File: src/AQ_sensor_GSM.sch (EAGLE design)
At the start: 102 parts, among them IC1 MIC29302WU, IC2 MCP73831/OT, J1 F-1X03-SIP-100-32, J3 PJ-002BH, J4 78646-3001, Q1 MMBT2222, Q2 MMBT2222, Q3 MMBT2222, Q4 MMBT2222, Q5 MMBT2222, Q6 MMBT2222, Q7 MMBT2222, U1 LM7805S/NOPB, U3 TEXAS_INSTRUMENTS_LM1117IMP-3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, U4 EC200UCNAB-N05-SNNSA, U5 TXS0108EPWR, X1 53048-08

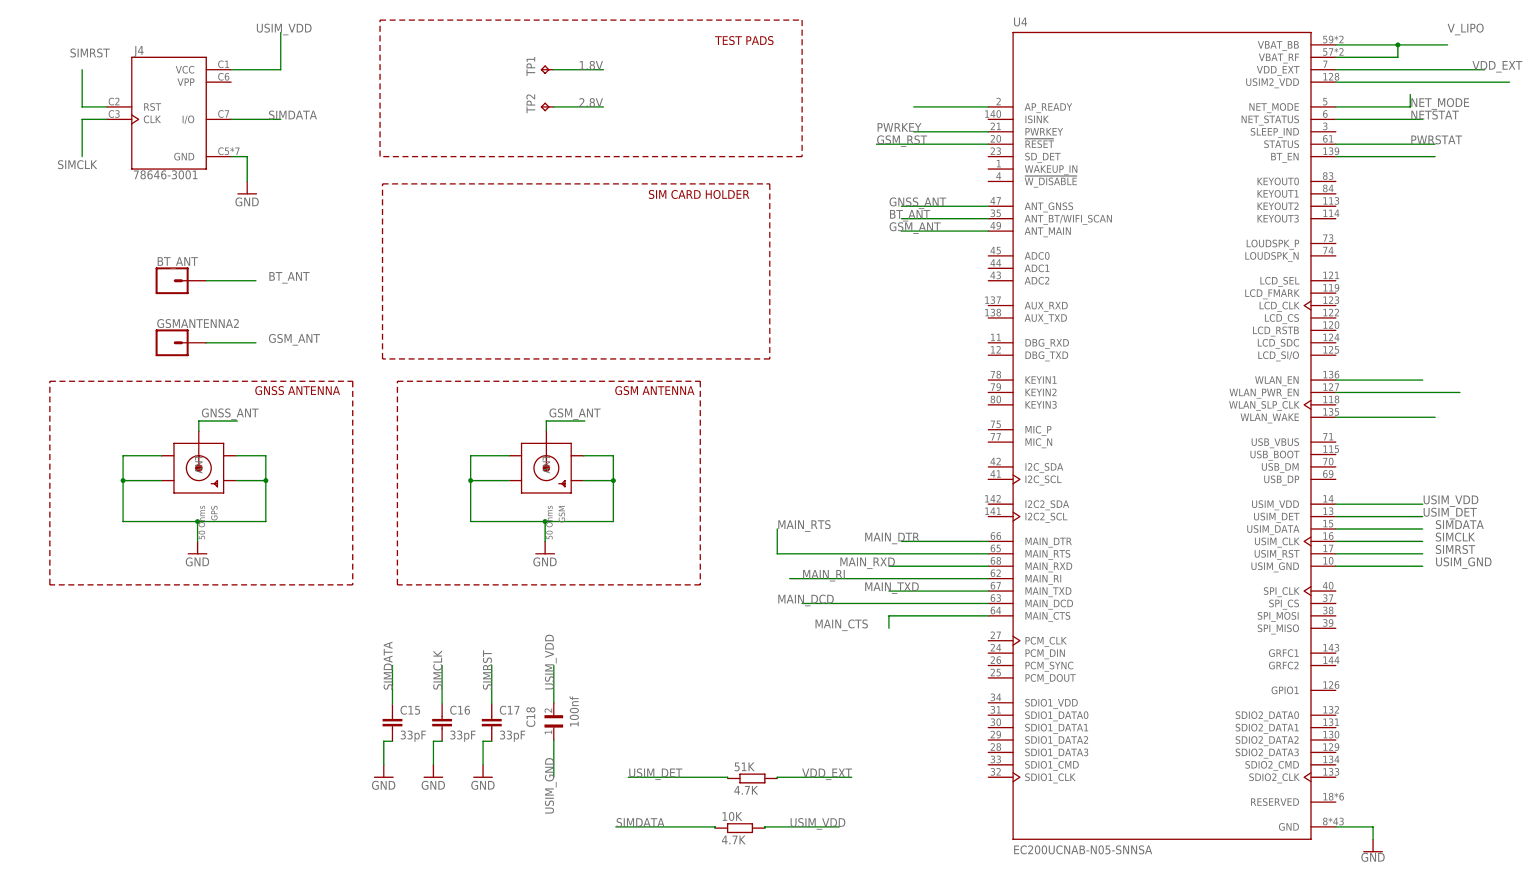
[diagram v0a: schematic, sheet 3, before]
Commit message: Replaced battery connector with 5.08mm terminal block
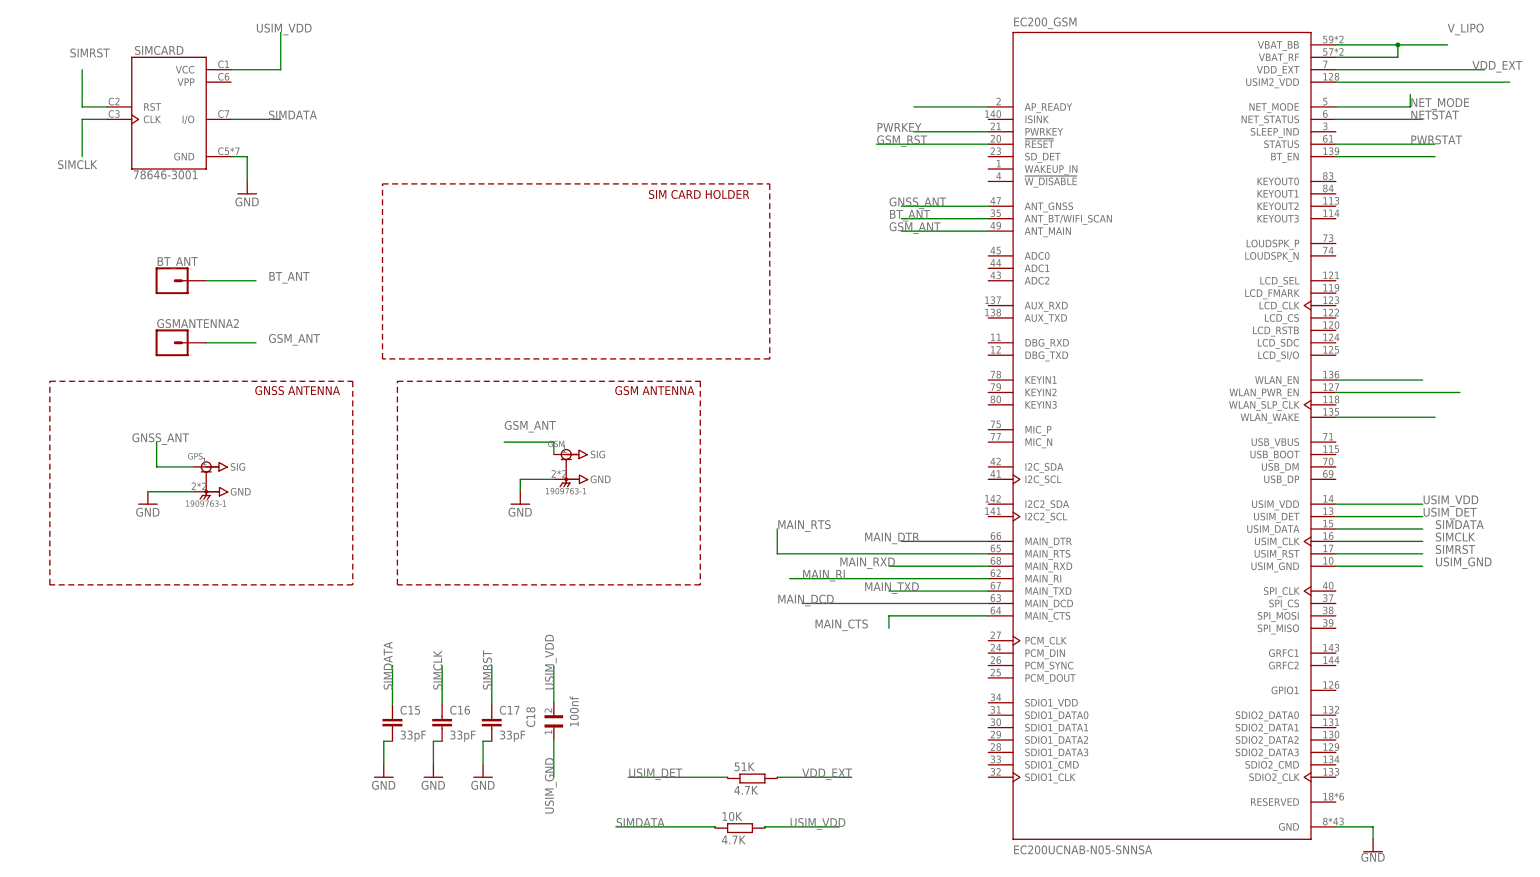
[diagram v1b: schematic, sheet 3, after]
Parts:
- removed CN1: (no value), AQ_sensor_GSM:JST_2PIN-SMT-RA
- removed TP1, TP2: TPB1,27, testpad:TPB1,27
- added 3.7V_LIPO: 2828XX-2282837-2, Connector:2828XX-2282837-2
- GPS, GSM: value 50 Ohms -> 1909763-1; device AQ_sensor_GSM:SMACONNECTOR_EDGE_UFL -> 1909763-1:1909763-1
- renumbered J4 to SIMCARD, U4 to EC200_GSM
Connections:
- removed net 1.8V: TP1.TP
- removed net 2.8V: TP2.TP
- net BP: now also 3.7V_LIPO.2; no longer CN1.2
- net GND: now also 3.7V_LIPO.1, GPS.GND, GSM.GND; no longer CN1.1, GPS.GND1, GPS.GND2, GPS.GND3, GPS.GND4, GSM.GND1, GSM.GND2, GSM.GND3, GSM.GND4
- net GNSS_ANT: now also GPS.SIG; no longer GPS.ANT
- net GSM_ANT: now also GSM.SIG; no longer GSM.ANT
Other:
- note removed: "TEST PADS"

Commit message: Added Lipo charging system
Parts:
- removed 3.7V_LIPO: 2828XX-2282837-2, Connector:2828XX-2282837-2
- removed C1, C4: 10uF, rcl:C-EUC0603
- removed CHRG: RED, led:LEDCHIP-LED0603
- removed FULL: YELLOW, led:LEDCHIP-LED0603
- removed IC2: MCP73831/OT, AQ_sensor_GSM:MCP73831/OT
- removed LIPO_SW, S1: TL2285EE, TL2285EE:TL2285EE
- removed MICRO_SD1: TF-01A, TF-01A:TF-01A
- removed MICRO_USB: 10118192-0001LF, AQ_sensor_GSM:10118192-0001LF
- removed U1: LM7805S/NOPB, LM7805S_NOPB:LM7805S/NOPB
- added 100%, 25%, 50%, 75%, C_P: ORANGE, led:LEDCHIP-LED0603
- added C14: 22nF, SparkFun-Capacitors:220PF-0402T-50V-5%
- added C21: 22pF, SparkFun-Capacitors:220PF-0402T-50V-5%
- added C22, C25, C26, C27, C5: ECA-1HM220, Resistor_Capacitor:ECA-1HM220
- added C23, C24, C29, C30: TAJB106K016RNJ, Resistor_Capacitor:TAJB106K016RNJ
- added CHARGE: PCM12SMTR, AQ_sensor_MRC:PCM12SMTR
- added L1: 784787047, Fixed Inductors:784787047
- added L2: 784778010, Fixed Inductors:784778010
- added LIPO: 2828XX-2282834-2, Connector:2828XX-2282834-2
- added LIPO/BUCK, USB/BATT: TL2285EE, TL2285EE:TL2285EE
- added PB_IN, SOLAR_IN: 10118192-0001LF, AQ_sensor_GSM:10118192-0001LF
- added R1: 110k, SparkFun-Resistors:1.20KOHM-0603-1/10W-1%
- added R37, R7: 10k, SparkFun-Resistors:1.20KOHM-0603-1/10W-1%
- added R6: 15, SparkFun-Resistors:1.20KOHM-0603-1/10W-1%
- added U$1: (no value), MT2492:MT2492MT2492
- added U$2: (no value), IP5306:IP5306IP5306
- R17, R19: value 470 -> 2R; device rcl:R-EU_R0603 -> SparkFun-Resistors:1.20KOHM-0603-1/10W-1%
- R20: value 2K -> 220R; device rcl:R-EU_R0603 -> SparkFun-Resistors:1.20KOHM-0603-1/10W-1%
- renumbered GSMANTENNA2 to GSM_ANT, M_RI to MRI, N_MODE to NMDE, N_STAT to NST, P_STAT to PST
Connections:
- removed net BP: 3.7V_LIPO.2, IC2.VBAT, LIPO_SW.NC1, LIPO_SW.NC2
- removed net CP: C6.1, C7.2, D5.K, IC1.OUT, LIPO_SW.NO1, LIPO_SW.NO2, R11.2, R9.2
- removed net JACKP: J3.1, U1.IN
- removed net N$12: FULL.A, R19.1
- removed net N$9: IC2.STAT, R17.2, R19.2
- removed net USBP: MICRO_USB.VUSB, S1.COM1, S1.COM2
- removed net VRTC: C4.1
- new net 3.8V: C6.1, C7.2, D5.K, IC1.OUT, LIPO/BUCK.NC1, LIPO/BUCK.NC2, R11.2, R9.2
- new net 4.2V: C29.1, L2.2, LIPO/BUCK.NO1, LIPO/BUCK.NO2, R19.2, U$2.BAT
- new net 5V_IN: C21.1, C22.1, C30.1, L1.2, R1.2, R17.2, U$2.VIN
- new net 5V_OUT: C25.1, C26.1, C27.1, U$2.VOUT, USB/BATT.NO1, USB/BATT.NO2
- new net BVIN: C5.1, J3.1, R7.2, SOLAR_IN.VUSB, U$1.VIN
- new net N$10: C21.2, R1.1, R6.2, U$1.FB
- new net N$11: R7.1, U$1.EN
- new net N$14: 100%.A, 25%.C, 50%.A, 75%.C, U$2.LED3
- new net N$17: 25%.A, 50%.C, U$2.LED1
- new net N$18: 100%.C, 75%.A, U$2.LED2
- new net N$20: CHARGE.1, R37.1
- new net N$21: L2.1, U$2.SW
- new net N$24: C24.1, R19.1
- new net N$3: C14.1, U$1.BS
- new net N$45: R20.2, R37.2, U$2.KEY
- new net N$46: C_P.A, R20.1
- new net VUSB: C2.1, C3.2, IC1.VIN, PB_IN.VUSB, R2.2, USB/BATT.NC1, USB/BATT.NC2
- net +3V3: no longer MICRO_SD1.VDD
- net +5V: now also USB/BATT.COM1, USB/BATT.COM2; no longer C1.1, C2.1, C3.2, CHRG.A, IC1.VIN, IC2.VDD, R2.2, S1.NO1, S1.NO2, U1.OUT
- net D+: now also PB_IN.D+, SOLAR_IN.D+; no longer MICRO_USB.D+
- net D-: now also PB_IN.D-, SOLAR_IN.D-; no longer MICRO_USB.D-
- net GND: now also C22.2, C23.2, C24.2, C25.2, C26.2, C27.2, C29.2, C30.2, C5.2, CHARGE.2, C_P.C, LIPO.2, PB_IN.GND, PB_IN.ID, PB_IN.SHIELD, R6.1, SOLAR_IN.GND, SOLAR_IN.ID, SOLAR_IN.SHIELD, U$1.GND, U$2.GND; no longer 3.7V_LIPO.1, C1.2, C4.2, FULL.C, IC2.VSS, MICRO_SD1.SHIELD, MICRO_SD1.VSS, MICRO_USB.GND, MICRO_USB.ID, MICRO_USB.SHIELD, R20.2, U1.GND
- net N$13: now also C23.1, R17.1; no longer IC2.PROG, R20.1
- net N$6: now also C14.2, L1.1, U$1.SW; no longer CHRG.C, R17.1
- net TF-CLK: no longer MICRO_SD1.CLK
- net TF-CS: no longer MICRO_SD1.CD/DAT3
- net TF-MISO: no longer MICRO_SD1.DAT0
- net TF-MOSI: no longer MICRO_SD1.CMD
- net V_LIPO: now also LIPO.1, LIPO/BUCK.COM1, LIPO/BUCK.COM2; no longer LIPO_SW.COM1, LIPO_SW.COM2
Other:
- note removed: "CHARGING CIRCUIT"
- note removed: "LIPO BATTERY"
- moved on the sheet: C10, C11, C12, C13, C2, C3, C6, C7, C9, D2, D5, J3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

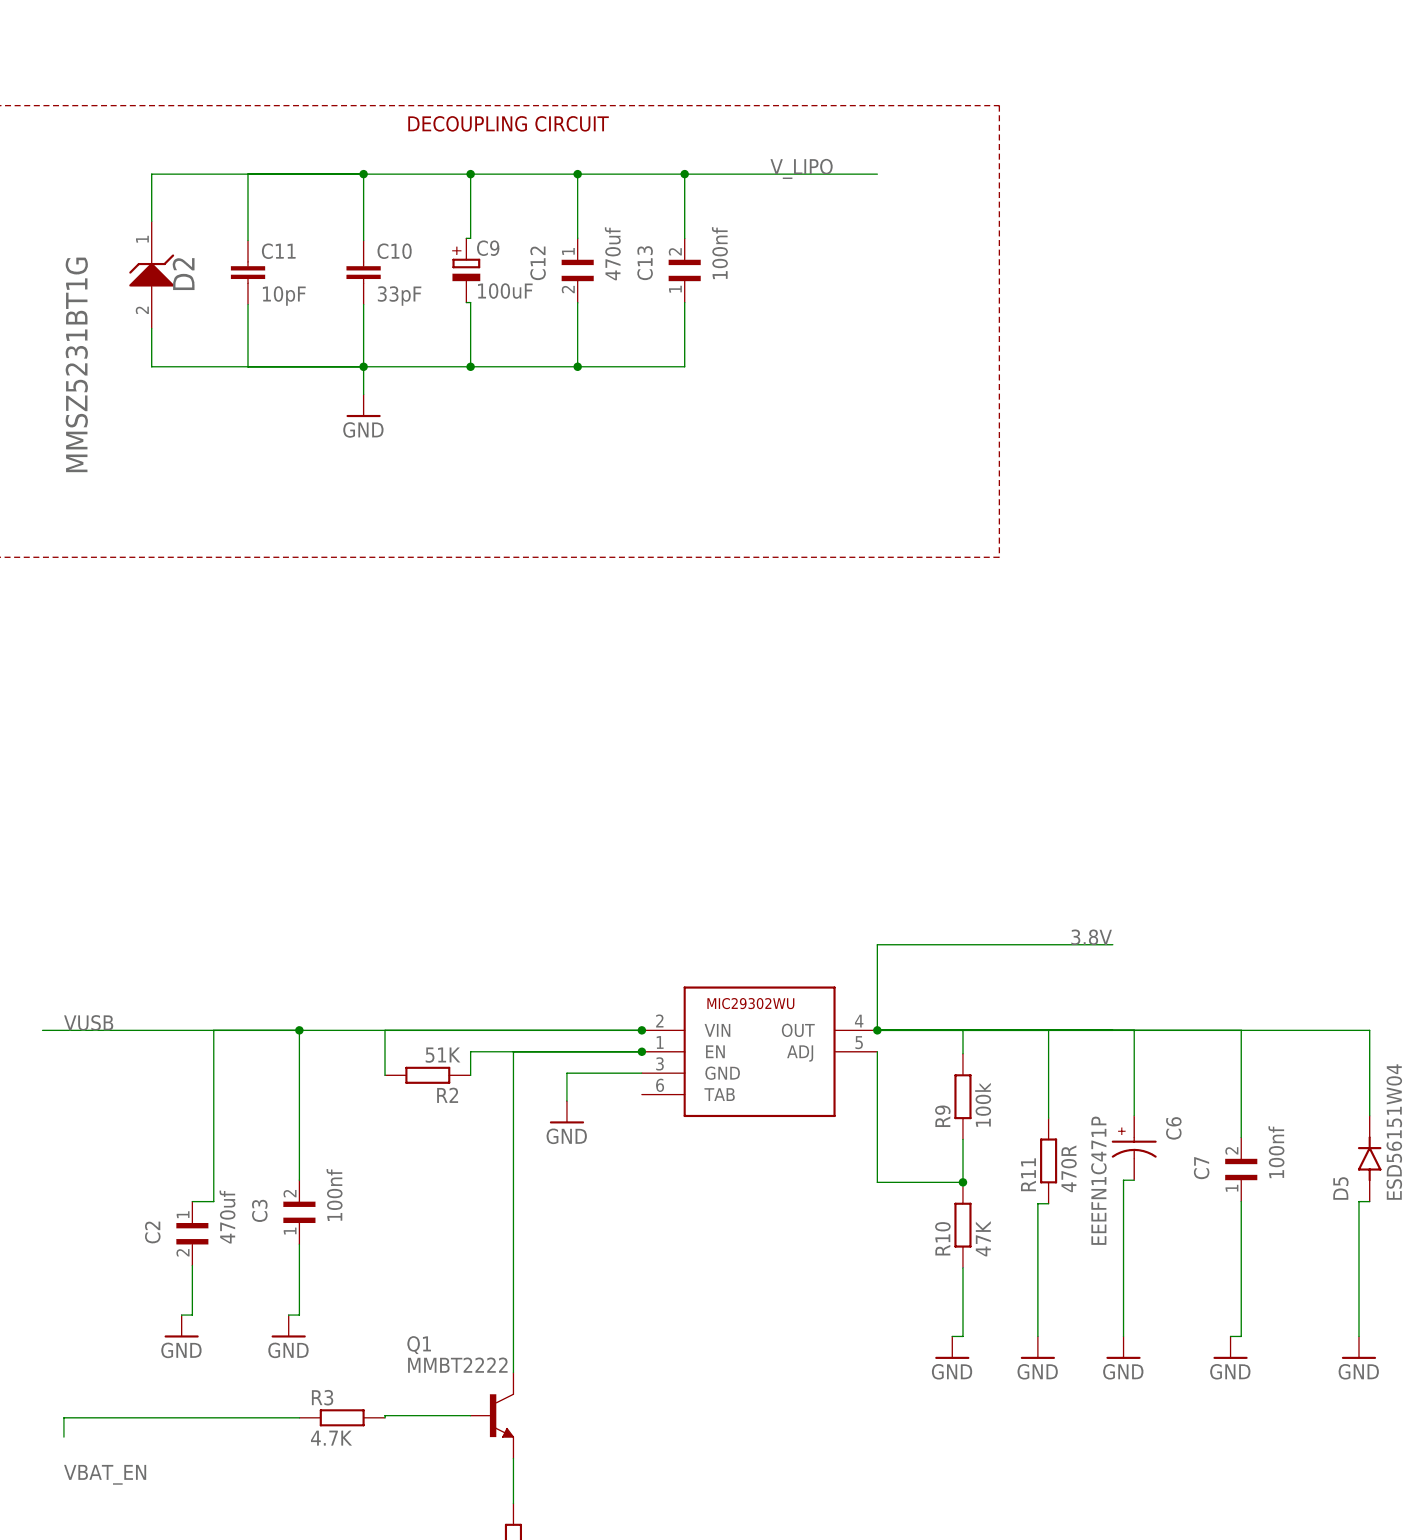
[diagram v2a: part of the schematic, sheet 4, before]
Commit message: Reordered components on the PCB, added Lipo charging circuit, added Charging level inidcator LED Bar.
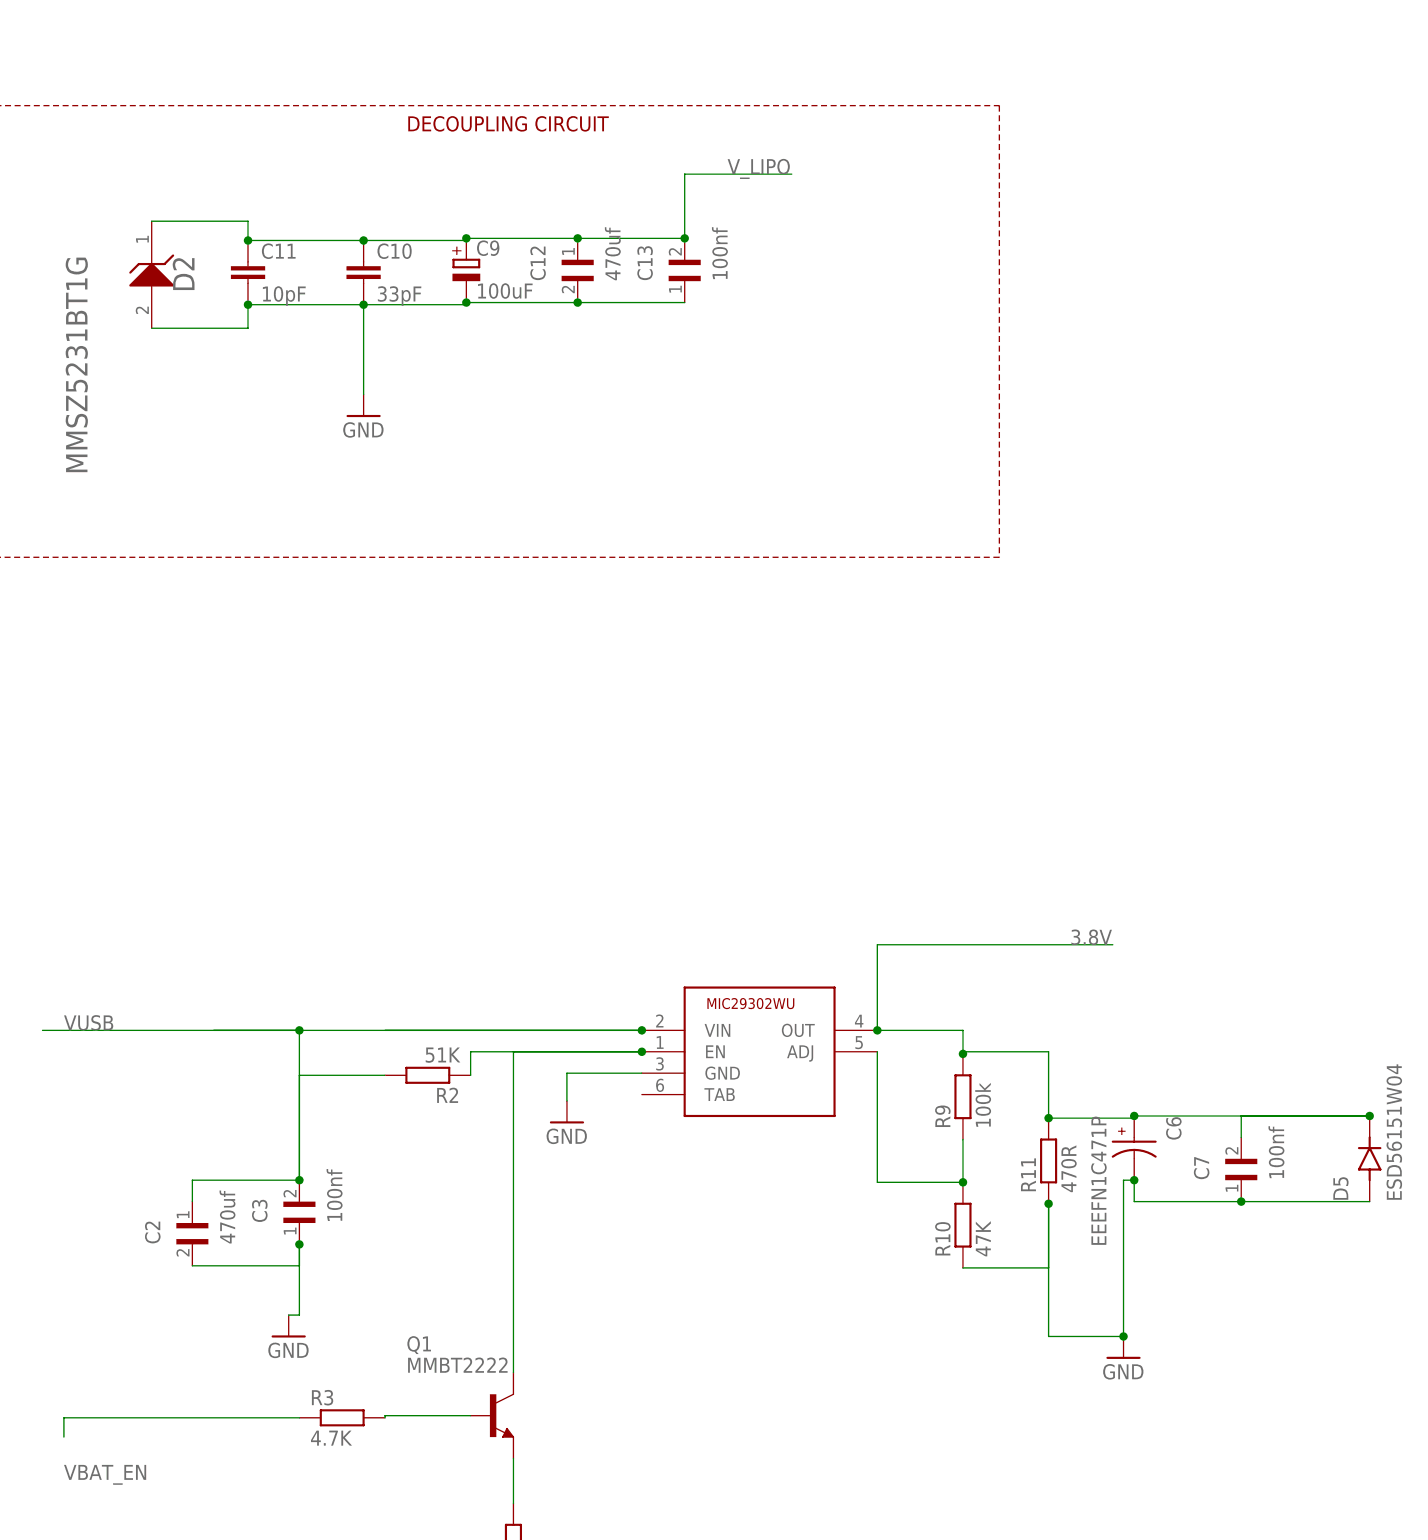
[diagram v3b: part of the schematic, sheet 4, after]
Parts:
- added C1: 10nF, SparkFun-Capacitors:10NF-0603-50V-10%
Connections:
- net GND: now also C1.2, D1.ANODE; no longer D1.CATHODE
- net GSM_RST: now also D1.CATHODE, GSM_RST.2
- net PWRKEY: now also C1.1; no longer D1.ANODE, GSM_RST.2
